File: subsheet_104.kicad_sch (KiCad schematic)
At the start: 6 parts

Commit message: update comments in cartridge
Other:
- title: Conversion du Thomson MO5 — Unité centrale v1 -> Conversion du Thomson MO5 — Unité centrale v2
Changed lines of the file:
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@@
   (paper "A4" portrait)
   (title_block
-    (title "Conversion du Thomson MO5 — Unité centrale v1")
-    (date "2024-12-30")
-    (rev "v1.0.0-rc2")
+    (title "Conversion du Thomson MO5 — Unité centrale v2")
+    (date "2025-02-08")
+    (rev "v2.0.0-alpha")
     (comment 1 "http://github.com/sporniket/kicad-conversions--thomson-mo5--v1")
-    (comment 3 "Gate Array Motorola MCA 1300 ALS")
-    (comment 4 "Reference : POP5001 501994-01")
+    (comment 3 "Gate Array EFCIS")
   )
   (junction (at 120.65 50.8) (diameter 0) (color 0 0 0 0)

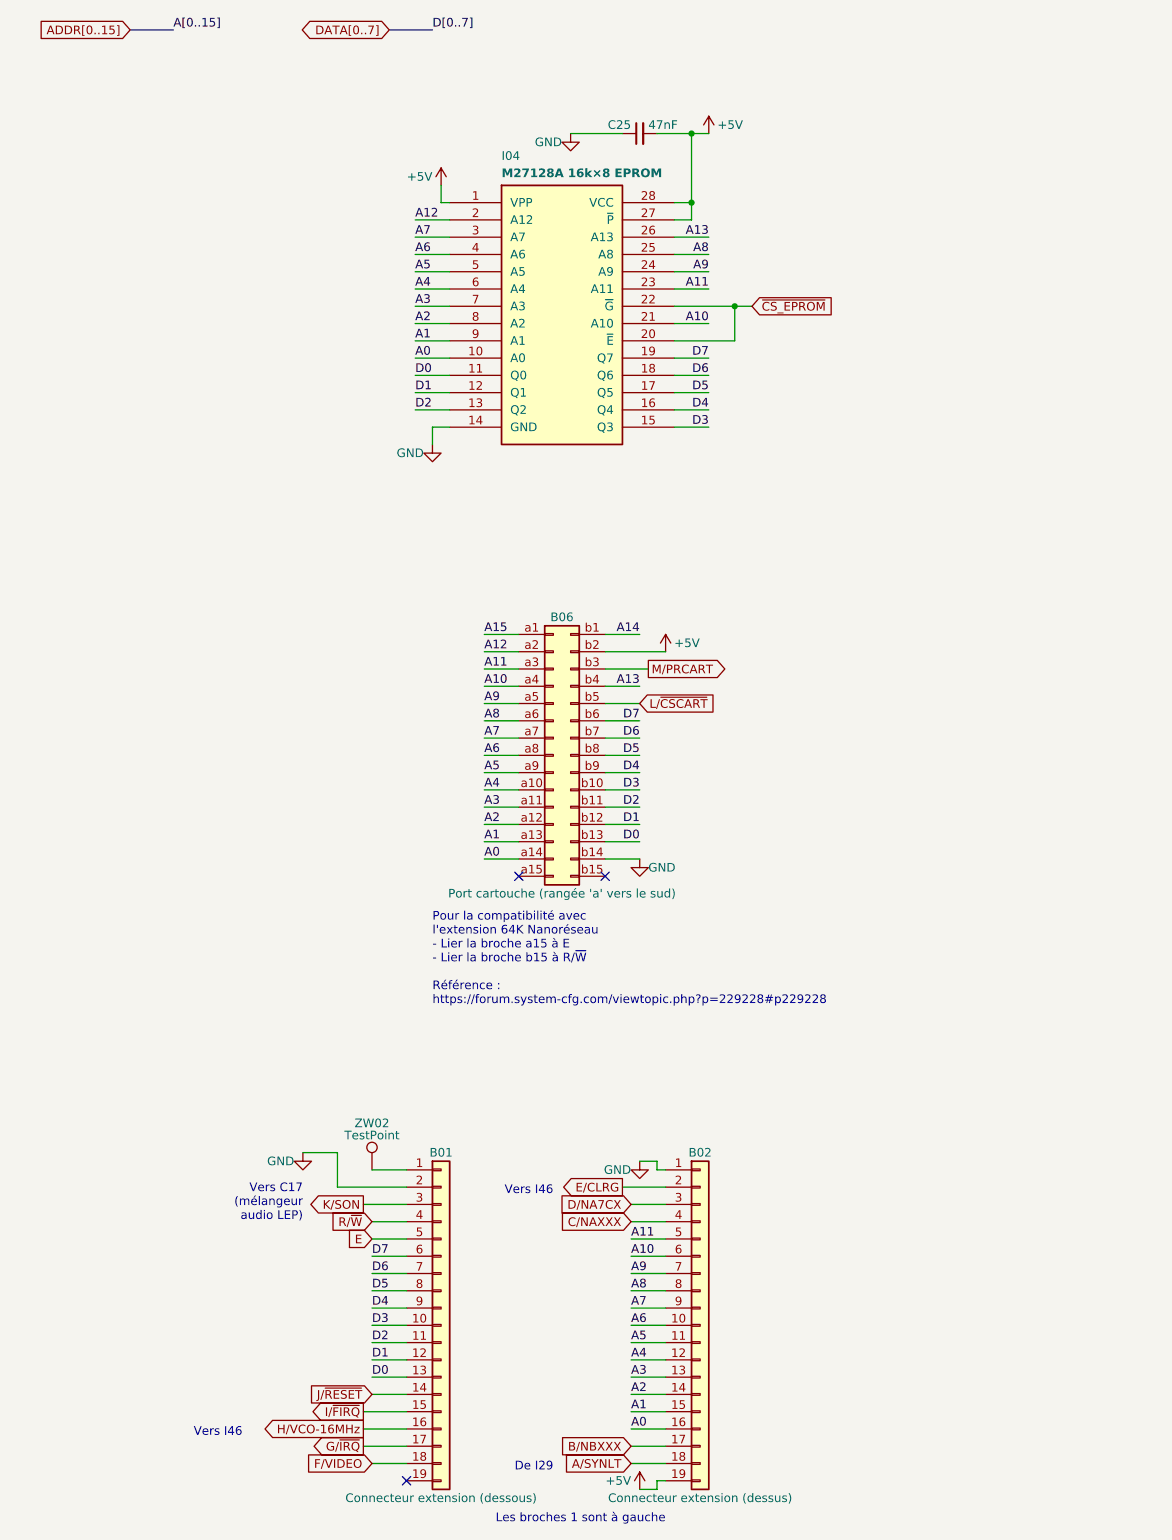
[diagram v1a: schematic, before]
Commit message: Resolves #16 : [ga efcis] Supplemental EPROM I56 (27c32) ; Fixed orientation and updated the cartridge port too
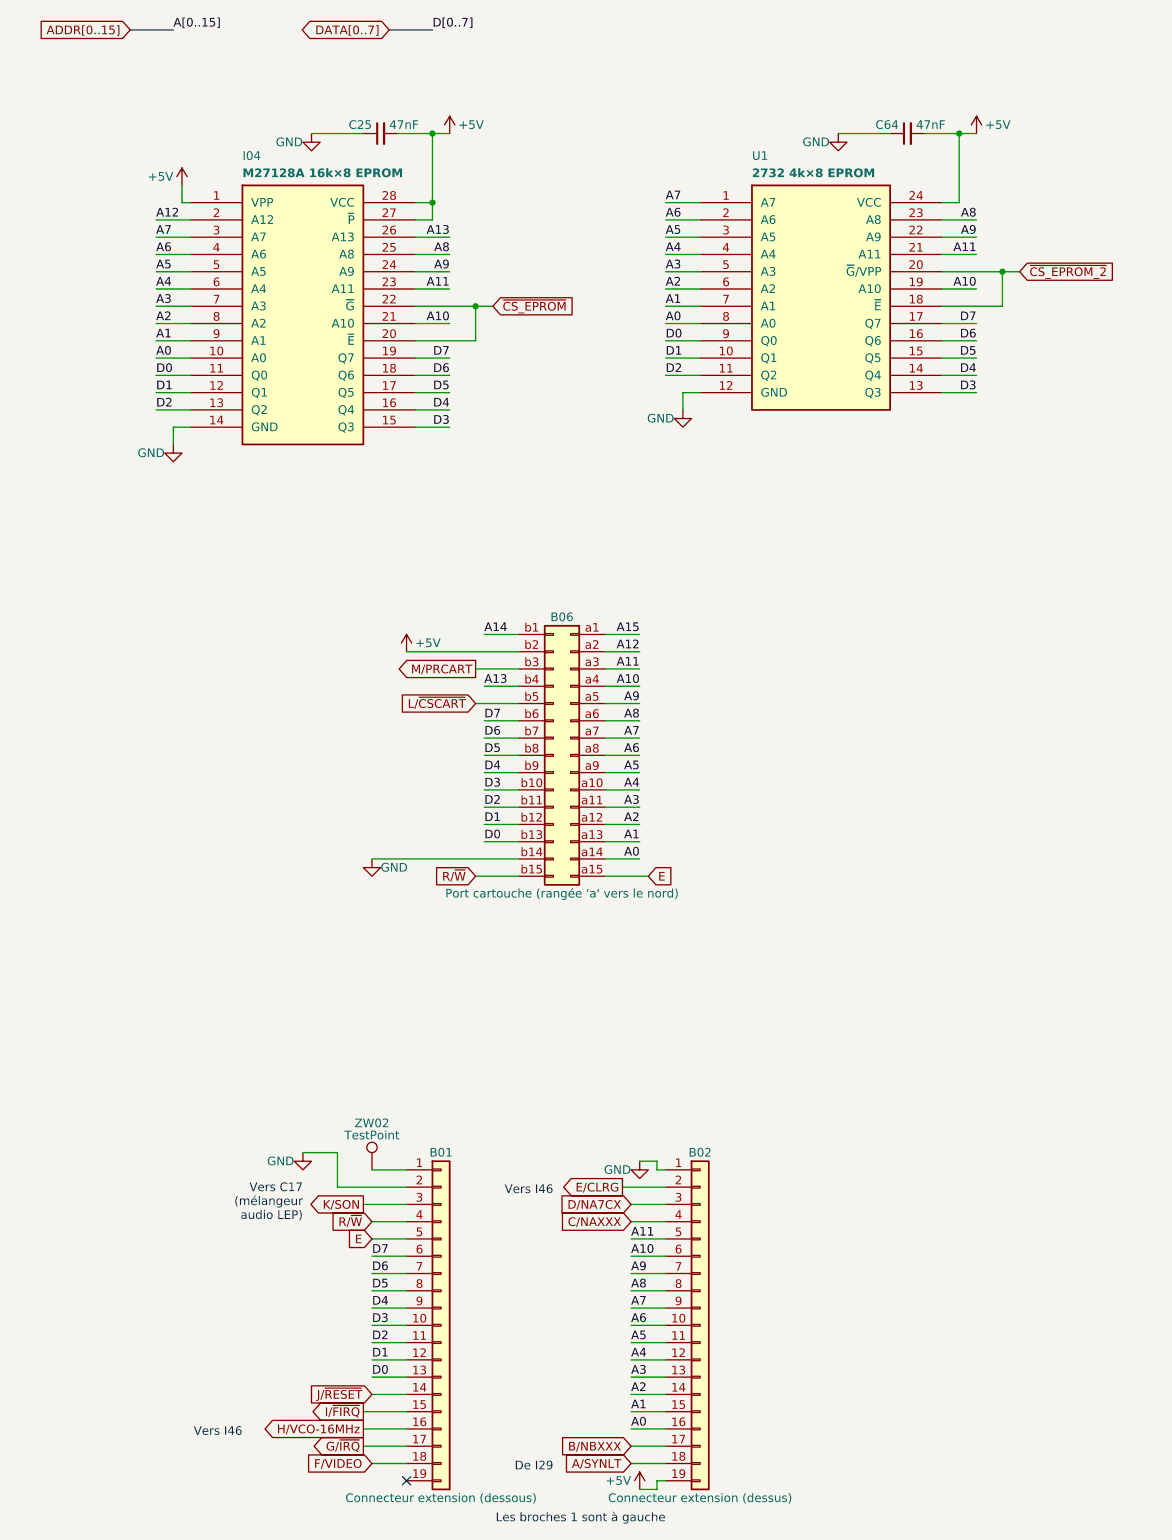
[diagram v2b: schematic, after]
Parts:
- added C64: 47nF, commons-passives_THT:Passive_THT_capacitor_mlcc_W2.54mm_L5.08mm, symbol Device:C_Small
- added U1: 2732 4k×8 EPROM, Package_DIP:DIP-24_W15.24mm_LongPads, symbol 27c32:32768-BIT_4096_X_8_CMOS_EPROM_PHY
- B06: value Port cartouche (rangée 'a' vers le sud) -> Port cartouche (rangée 'a' vers le nord)
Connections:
- net +5V: now also C64.2, U1.24 (VCC)
- net A0: now also U1.8 (A0)
- net A1: now also U1.7 (A1)
- net A10: now also U1.19 (A10)
- net A11: now also U1.21 (A11)
- net A2: now also U1.6 (A2)
- net A3: now also U1.5 (A3)
- net A4: now also U1.4 (A4)
- net A5: now also U1.3 (A5)
- net A6: now also U1.2 (A6)
- net A7: now also U1.1 (A7)
- net A8: now also U1.23 (A8)
- net A9: now also U1.22 (A9)
- net D0: now also U1.9 (Q0)
- net D1: now also U1.10 (Q1)
- net D2: now also U1.11 (Q2)
- net D3: now also U1.13 (Q3)
- net D4: now also U1.14 (Q4)
- net D5: now also U1.15 (Q5)
- net D6: now also U1.16 (Q6)
- net D7: now also U1.17 (Q7)
- net E: now also B06.a15 (Pin_a15)
- net GND: now also C64.1, U1.12 (GND)
- net R/~{W}: now also B06.b15 (Pin_b15)
- new net ~{CS_EPROM_2}: U1.18 (~{E}), U1.20 (~{G}/VPP)
- no-connect marks 3 -> 1
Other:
- note removed: "Pour la compatibilité avec l'extension 64K Nanoréseau - Lier la broche a15 à E - Lier la broche b15 à R/~{W} Référence : https://forum.system-cfg.com/viewtopic.php?p=229228#p229228"
- moved on the sheet: C25, I04

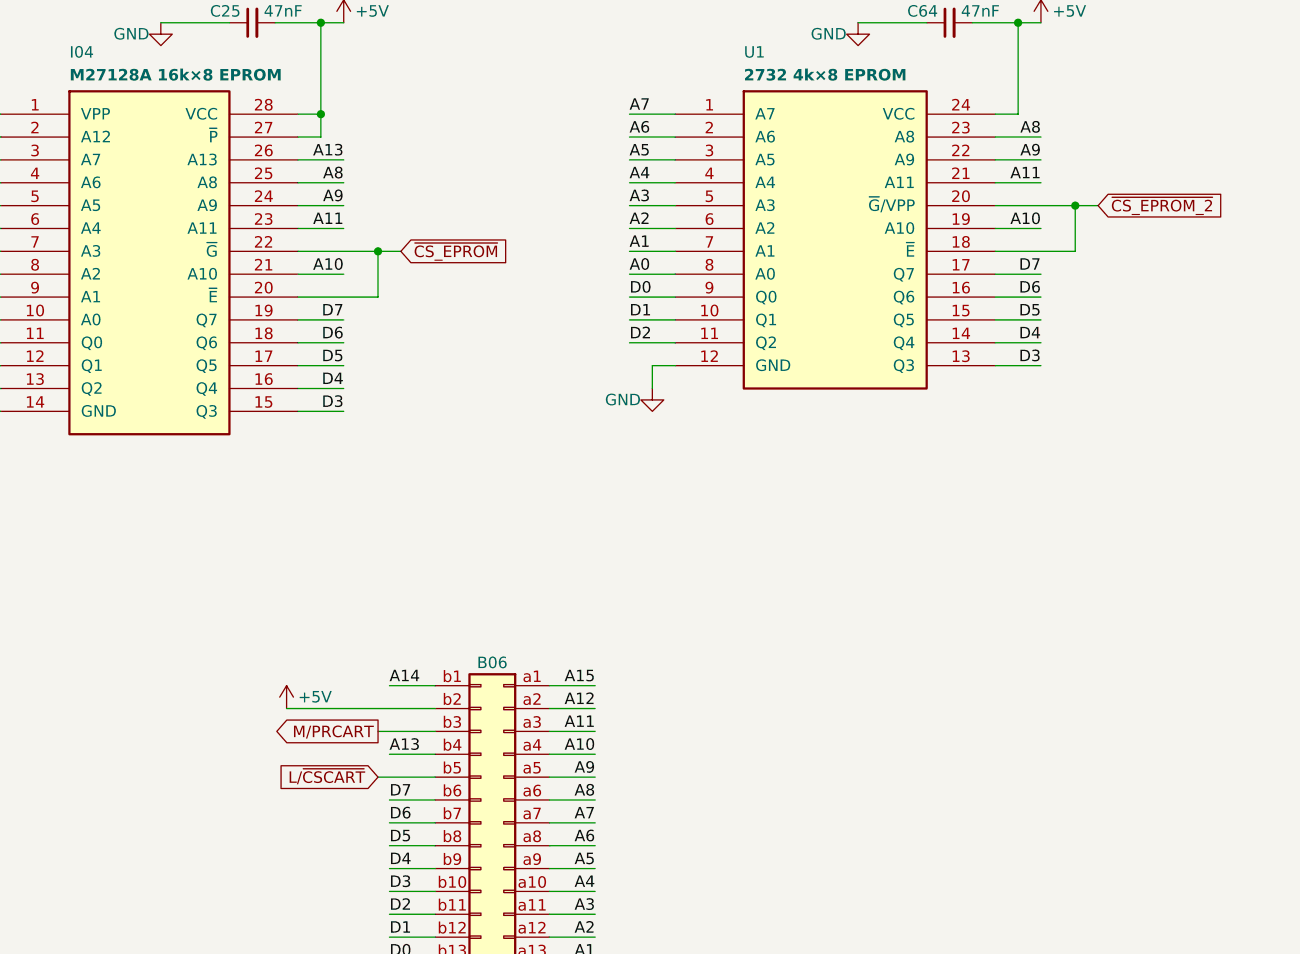
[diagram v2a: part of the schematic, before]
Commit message: Various mentions, added C60bis to I29 on pin 62
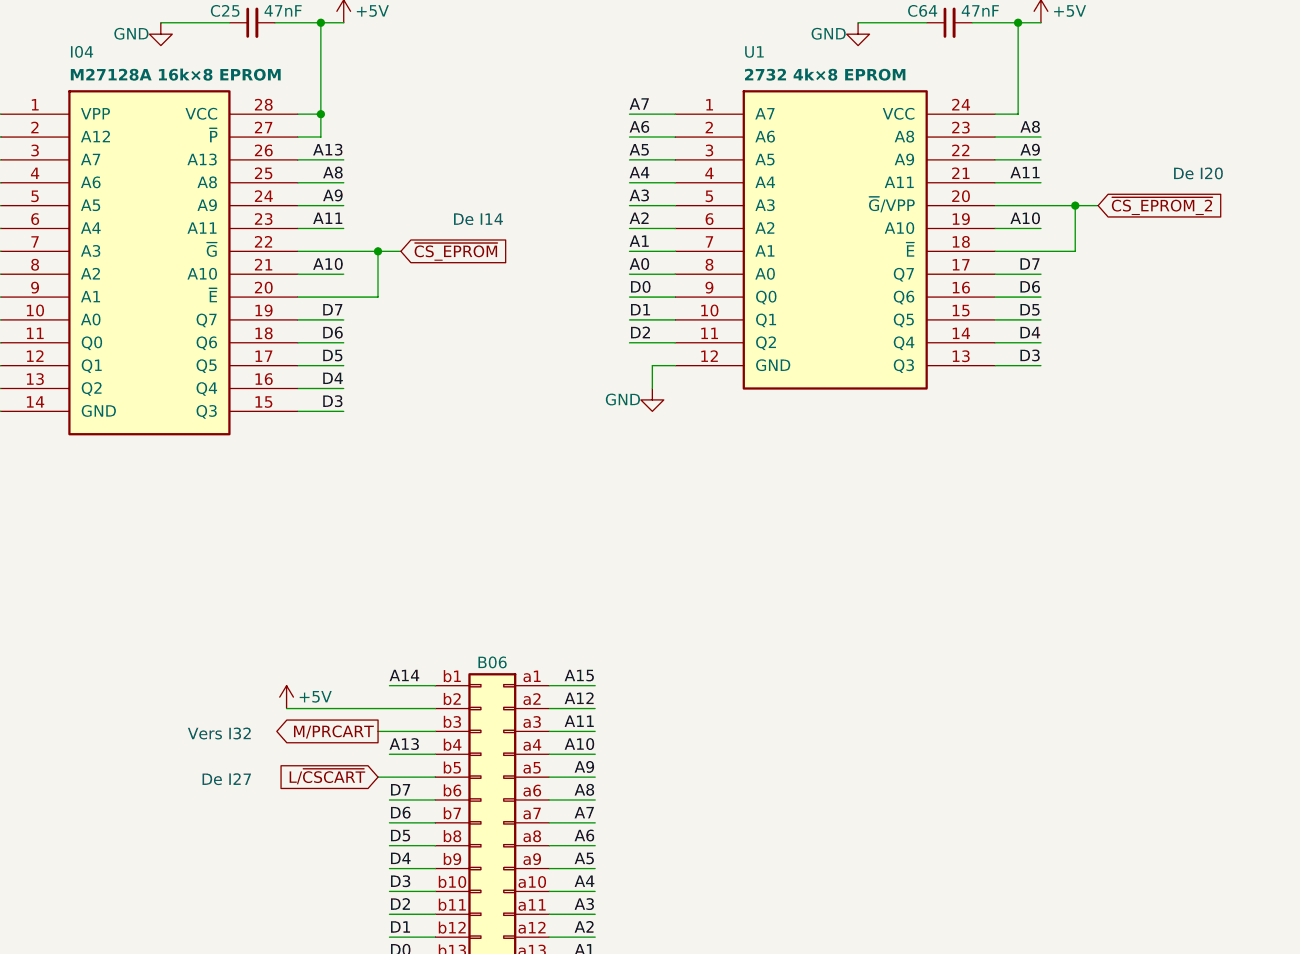
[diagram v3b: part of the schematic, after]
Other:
- note added: "De I14"
- note added: "De I20"
- note added: "De I27"
- note added: "Vers I32"
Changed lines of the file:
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@@
     (stroke (width 0) (type default))
+  )
+  (text "De I27" (at 74.93 125.73 0)
+    (effects (font (size 1.27 1.27)) (justify right bottom))
+  )
+  (text "De I14" (at 102.87 63.5 0)
+    (effects (font (size 1.27 1.27)) (justify right bottom))
+  )
+  (text "Vers I32" (at 74.93 120.65 0)
+    (effects (font (size 1.27 1.27)) (justify right bottom))
   )
   (text "Vers I46" (at 100.33 196.85 0)
@@
     (effects (font (size 1.27 1.27)) (justify right bottom))
   )
+  (text "De I20" (at 182.88 58.42 0)
+    (effects (font (size 1.27 1.27)) (justify right bottom))
+  )

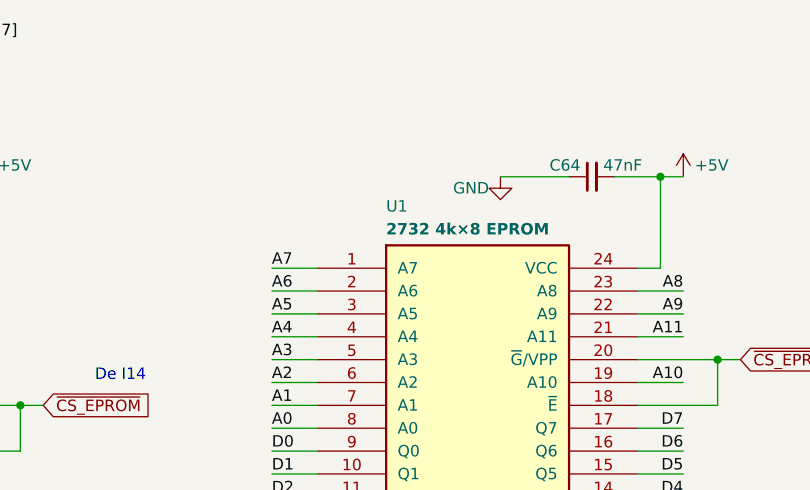
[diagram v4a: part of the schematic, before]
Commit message: fixes second EPROM designator, name of subsheet 104
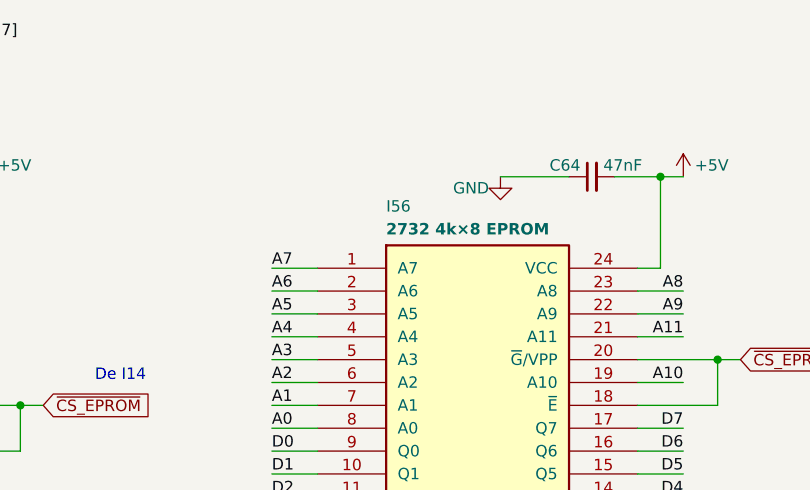
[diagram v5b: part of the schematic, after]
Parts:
- renumbered U1 to I56
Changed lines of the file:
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@@
   (symbol (lib_id "27c32:32768-BIT_4096_X_8_CMOS_EPROM_PHY") (at 139.7 64.77 0) (unit 1)
     (in_bom yes) (on_board yes) (dnp no)
-    (property "Reference" "U1" (at 129.54 43.18 0)
+    (property "Reference" "I56" (at 129.54 43.18 0)
       (effects (font (size 1.27 1.27)) (justify left top))
     )
@@
       (project "UC-50-001"
         (path "/e63e39d7-6ac0-4ffd-8aa3-1841a4541b55/ecfd8528-d7bf-4f5f-9e5b-93e6e3949e61"
-          (reference "U1") (unit 1)
+          (reference "I56") (unit 1)
         )
       )
